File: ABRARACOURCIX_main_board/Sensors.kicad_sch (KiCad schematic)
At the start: 12 parts, among them U2 BNO055, Y1 ABS07-32.768KHZ-T

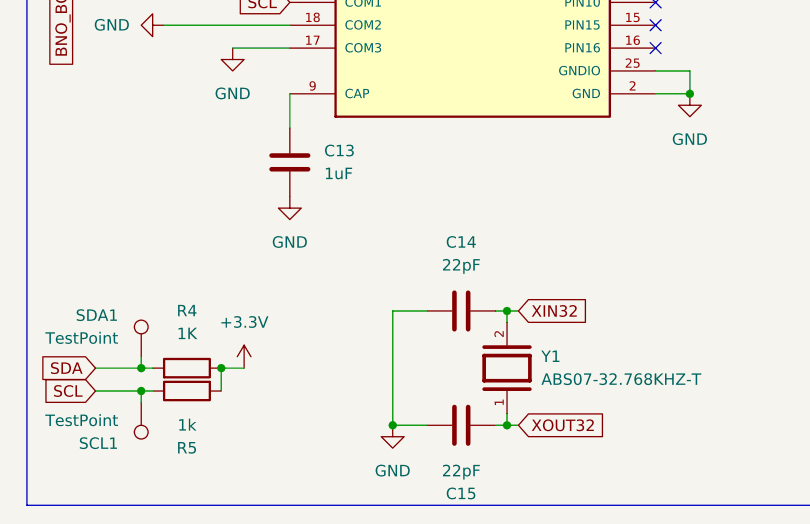
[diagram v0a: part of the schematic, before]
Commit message: Documentation, lien digikey et part number assigné à toutes les composantes
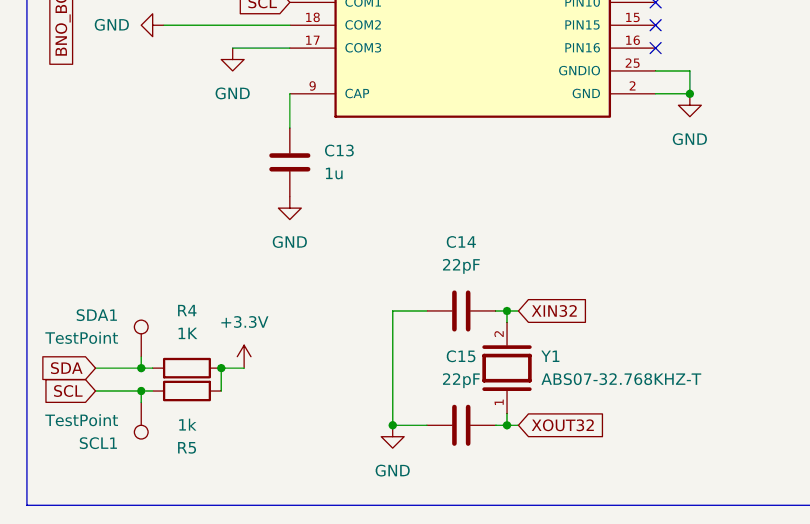
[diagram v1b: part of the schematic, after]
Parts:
- C12: Digikey (none) -> https://www.digikey.ca/en/products/detail/walsin-technology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; Part number (none) -> 1292-1605-1-ND
- C13: value 1uF -> 1u; Digikey (none) -> https://www.digikey.ca/en/products/detail/walsin-technology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; Part number (none) -> 1292-1206B105K250CT-ND
- C14, C15: Digikey (none) -> https://www.digikey.ca/en/products/detail/kemet/C1206C220K1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; Part number (none) -> 399-C1206C220K1GACTUCT-ND
- R2, R3: Digikey (none) -> https://www.digikey.ca/en/products/detail/bourns-inc/CR1206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; Part number (none) -> CR1206-JW-103ELFCT-ND
- R4, R5: Digikey (none) -> https://www.digikey.ca/en/products/detail/bourns-inc/CR1206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; Part number (none) -> 118-CR1206-JW-102ELFCT-ND
- SCL1, SDA1: now left out of the parts list
- U2: Digikey (none) -> https://www.digikey.ca/en/products/detail/bosch-sensortec/B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; Part number (none) -> 828-1058-1-ND
- Y1: Digikey (none) -> https://www.digikey.ca/en/products/detail/abracon-llc/ABS07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; Part number (none) -> 535-9542-1-ND
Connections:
- net GND: now also C15.2; no longer C15.1
- net XOUT32: now also C15.1; no longer C15.2
